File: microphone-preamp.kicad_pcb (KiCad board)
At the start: 2 copper layers, 47.5 x 67.5 mm, 47 parts, among them J1 LED, J2 PHANTOM POWER, J3 MIC XLR, J4 PHANTOM POWER SW, J5 GAIN 10k, J6 OUT, J7 POWER, U1 INA217, U2 TL071

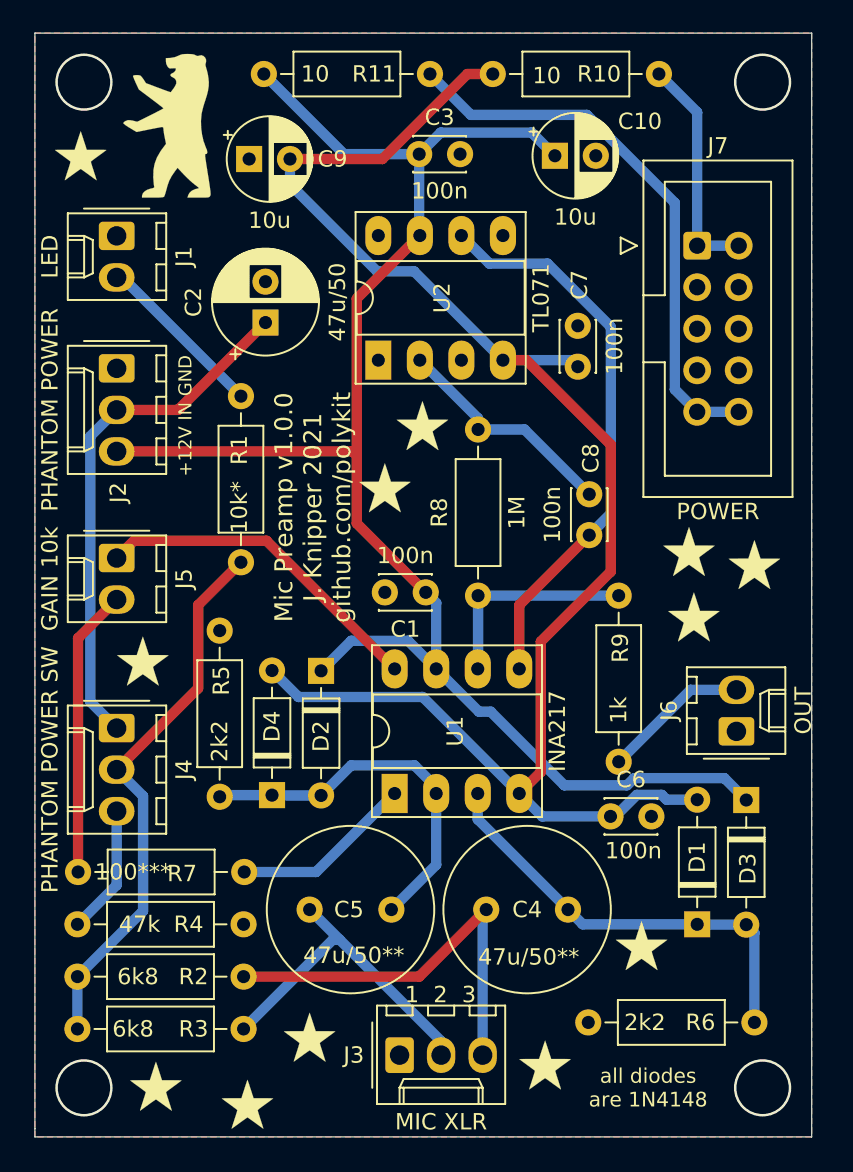
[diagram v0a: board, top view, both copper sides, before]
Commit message: Fix silkscreen, readme
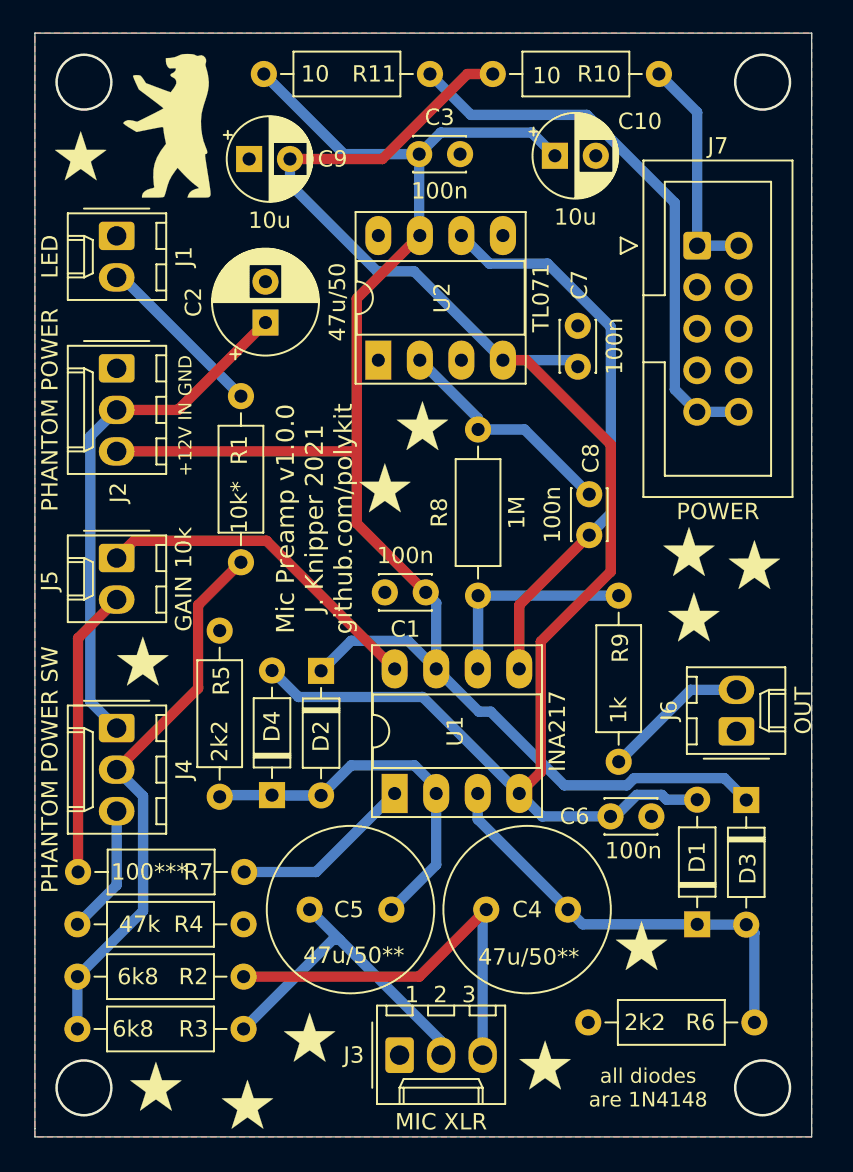
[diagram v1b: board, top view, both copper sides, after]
